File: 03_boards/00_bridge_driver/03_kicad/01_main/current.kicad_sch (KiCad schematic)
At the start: 20 parts, among them U12 AMC1311, U13 AMC1311

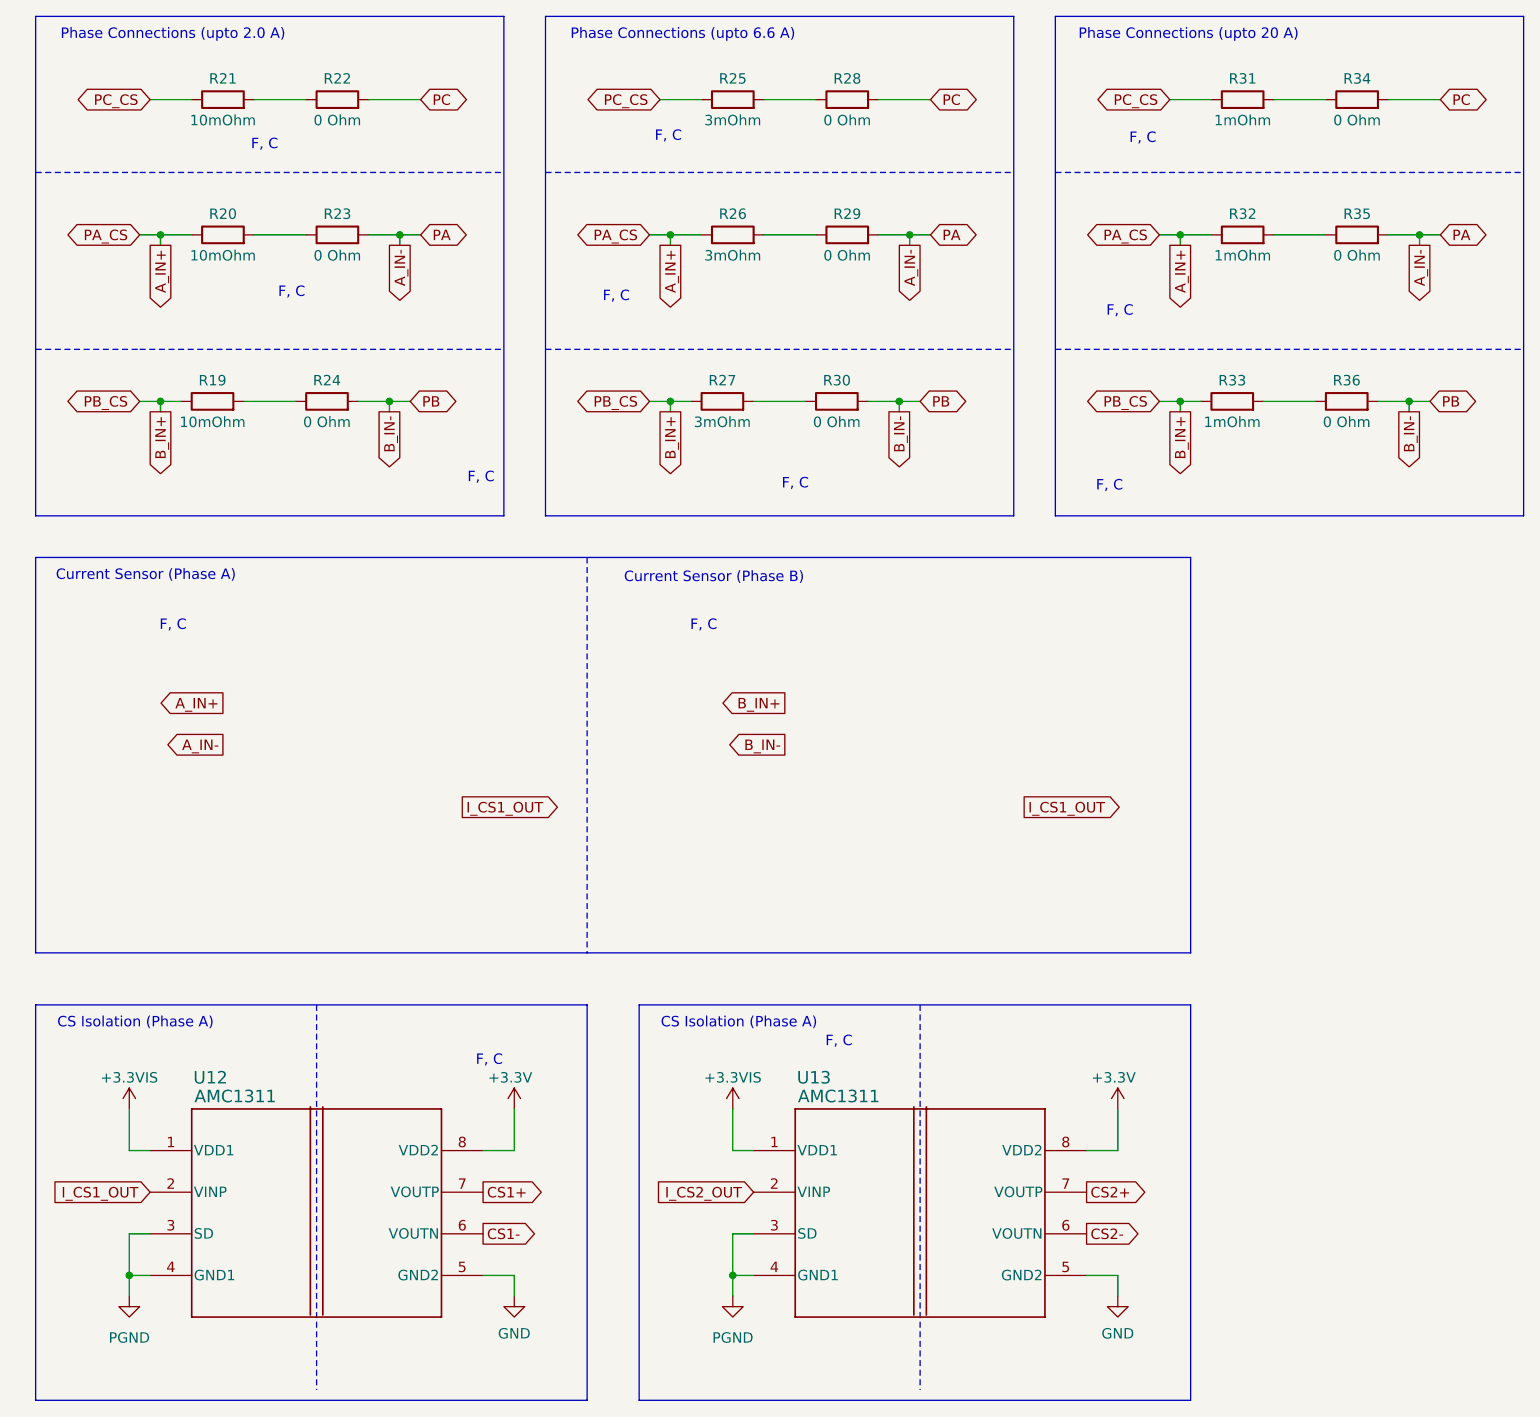
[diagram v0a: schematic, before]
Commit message: Nearly finished the schematic for driver board
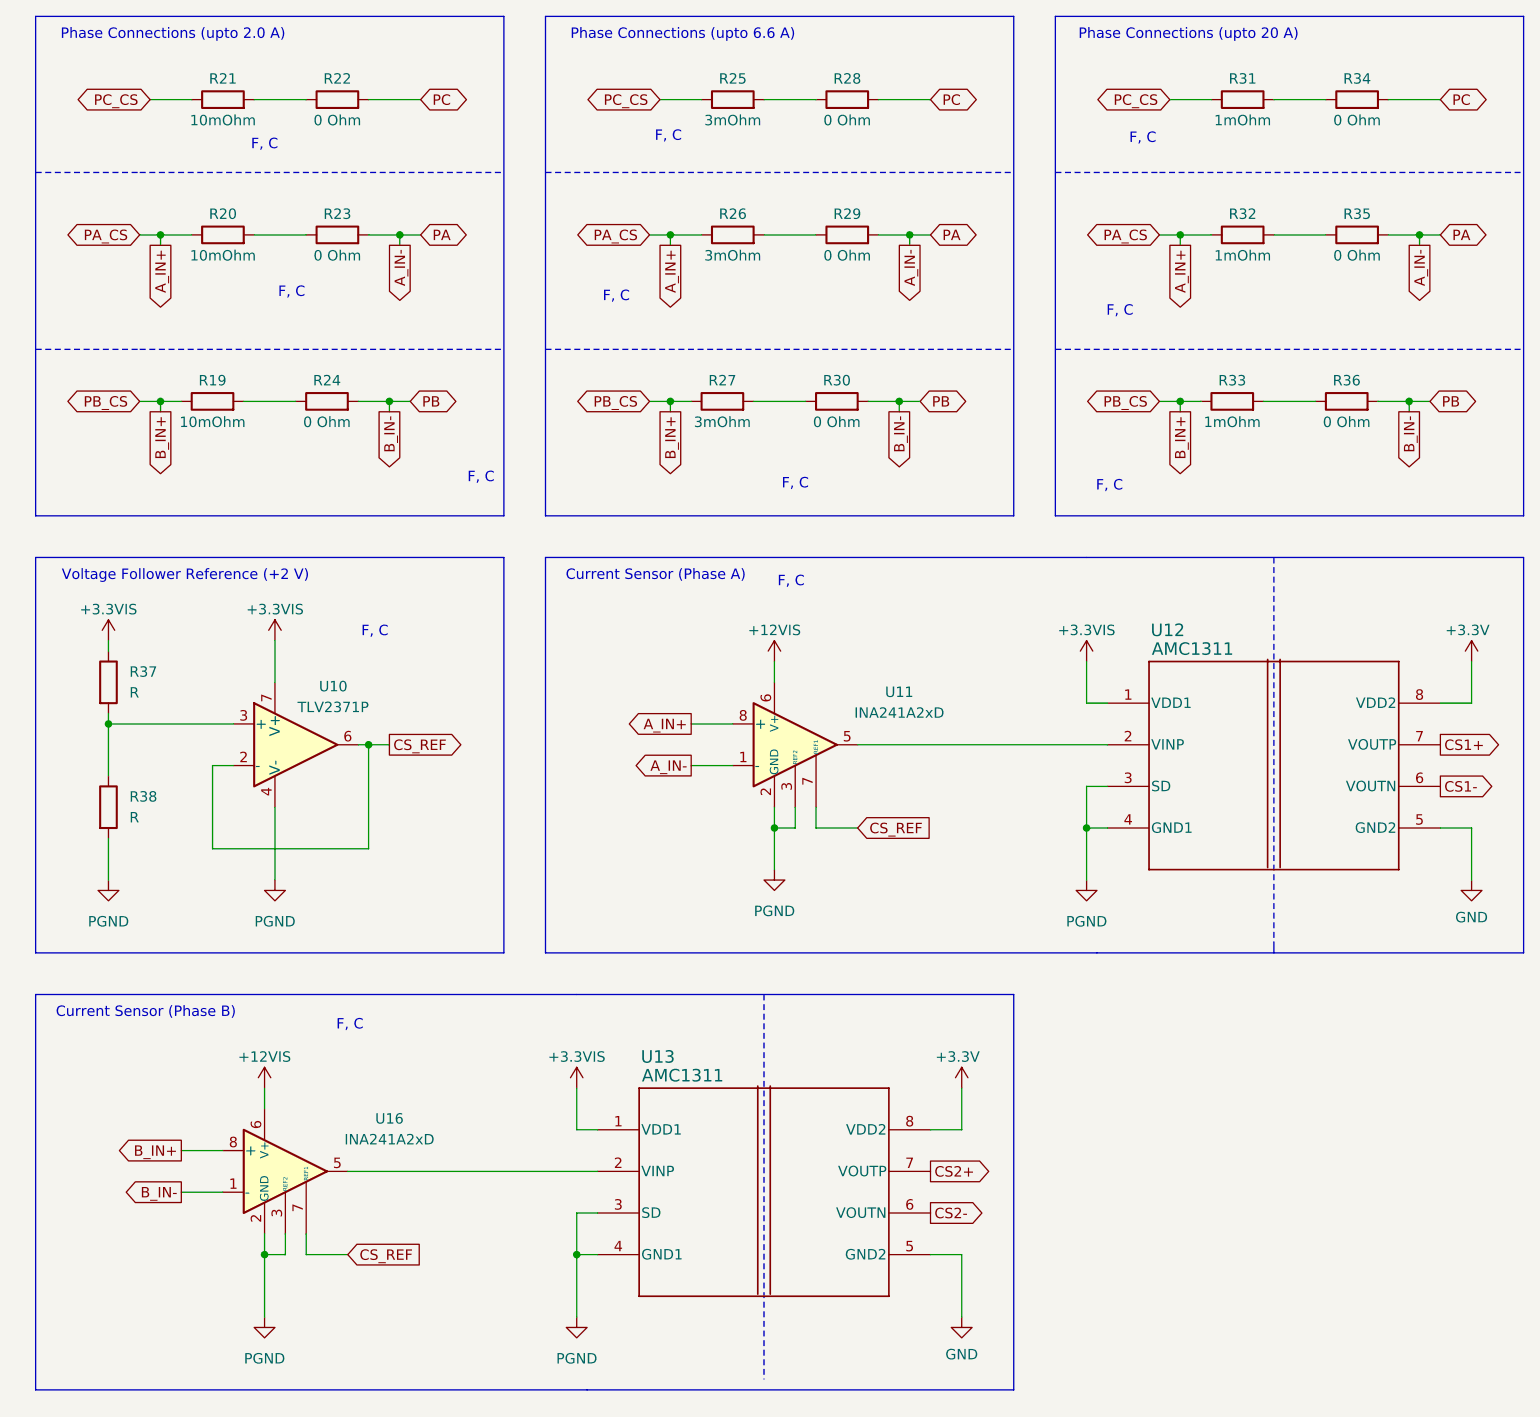
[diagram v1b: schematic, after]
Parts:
- added R37, R38: R, symbol Device:R
- added U10: TLV2371P, Package_DIP:DIP-8_W7.62mm, symbol Amplifier_Operational:TLV2371P
- added U11, U16: INA241A2xD, Package_SO:SOIC-8_3.9x4.9mm_P1.27mm, symbol Amplifier_Current:INA241A2xD
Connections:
- net +3.3VIS: now also R37.1, U10.7 (V+)
- net A_IN+: now also U11.8 (+)
- net A_IN-: now also U11.1 (-)
- net B_IN+: now also U16.8 (+)
- net B_IN-: now also U16.1 (-)
- net PGND: now also R38.2, U10.4 (V-), U11.2 (GND), U11.3 (REF2), U11.4 (GND), U16.2 (GND), U16.3 (REF2), U16.4 (GND)
- net I_CS1_OUT: no longer names the net of U12.2 (VINP)
- net I_CS1_OUT: now also U11.5
- net I_CS2_OUT: no longer names the net of U13.2 (VINP)
- net I_CS2_OUT: now also U16.5
- new net: R37.2, R38.1, U10.3 (+)
- new net +12VIS: U11.6 (V+), U16.6 (V+)
- new net CS_REF: U10.2 (-), U10.6, U11.7 (REF1), U16.7 (REF1)
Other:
- note added: "Voltage Follower Reference (+2 V)"
- note removed: "CS Isolation (Phase A)"
- moved on the sheet: U12, U13

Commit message: Finished Driver Board Schematic.
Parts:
- removed R37, R38: R, symbol Device:R
- removed U10: TLV2371P, Package_DIP:DIP-8_W7.62mm, symbol Amplifier_Operational:TLV2371P
- added C28: 10uF, symbol Device:C
- added U10: REF3020, Package_TO_SOT_SMD:SOT-23, symbol Reference_Voltage:REF3020
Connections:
- net +3.3VIS: now also C28.1, U10.1 (IN)
- net CS_REF: now also U10.2 (OUT)
- net PGND: now also C28.2, U10.3 (GND)

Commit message: More footprint selection. YAY
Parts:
- R19, R20, R21, R22, R23, R24, R25, R26, R27, R28, R29, R30, R31, R32, R33, R34, R35, R36: footprint (none) -> Resistor_SMD:R_2512_6332Metric
- U12, U13: footprint DWV0008A -> AMC1311DWVR:DWV0008A
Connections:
- net A_IN-: now also R20.2, R23.1, R26.2, R29.1, R32.2, R35.1; no longer R23.2, R29.2, R35.2
- net B_IN-: now also R19.2, R24.1, R27.2, R30.1, R33.2, R36.1; no longer R24.2, R30.2, R36.2
- new net PA: R23.2, R29.2, R35.2
- new net PB: R24.2, R30.2, R36.2
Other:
- note removed: "F, C"
- moved on the sheet: R22, R23, R24, R28, R29, R30, R34, R35, R36

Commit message: Footprints finished and hence initial BOM based on footprints is also
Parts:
- C28: footprint (none) -> Capacitor_SMD:C_1206_3216Metric
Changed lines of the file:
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@@
 			)
 		)
-		(property "Footprint" ""
+		(property "Footprint" "Capacitor_SMD:C_1206_3216Metric"
 			(at 25.0952 113.03 0)
 			(hide yes)

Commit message: Made it clear the values and updated the schematics.
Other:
- note added: "Phase Connections (upto 16.6 A (PEAK))"
- note added: "Phase Connections (upto 30 A (PEAK))"
- note added: "Phase Connections (upto 5.0 A (PEAK))"
- note removed: "Phase Connections (upto 2.0 A)"
- note removed: "Phase Connections (upto 20 A)"
- note removed: "Phase Connections (upto 6.6 A)"
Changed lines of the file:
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@@
 		(rev "0")
 	)
-	(text "Phase Connections (upto 20 A)\n"
+	(text "Phase Connections (upto 30 A (PEAK))\n"
 		(exclude_from_sim no)
-		(at 157.226 18.796 0)
+		(at 161.036 18.796 0)
 		(effects
 			(font
@@
 		)
 	)
-	(text "Phase Connections (upto 2.0 A)\n"
+	(text "Phase Connections (upto 5.0 A (PEAK))\n"
 		(exclude_from_sim no)
-		(at 33.274 18.796 0)
+		(at 36.83 18.796 0)
 		(effects
 			(font
@@
 		)
 	)
-	(text "Phase Connections (upto 6.6 A)\n"
+	(text "Phase Connections (upto 16.6 A (PEAK))\n"
 		(exclude_from_sim no)
-		(at 95.504 18.796 0)
+		(at 99.822 18.796 0)
 		(effects
 			(font

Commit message: Initial PCB modelling work
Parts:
- removed R22, R23, R24, R28, R29, R30, R34, R35, R36: 0 Ohm, Resistor_SMD:R_2512_6332Metric, symbol Device:R
- removed R25, R26, R27: 3mOhm, Resistor_SMD:R_2512_6332Metric, symbol Device:R
- removed R31, R32, R33: 1mOhm, Resistor_SMD:R_2512_6332Metric, symbol Device:R
- R19, R20, R21: value 10mOhm -> 5mOhm
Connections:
- net PC_CS is gone; now on net C_IN+: R21.1
- net PB: now also R19.2
- net C_IN-: now reaches R21.2
- net C_IN-: now also U16.1 (-)
- net B_IN+ renamed C_IN+
- net C_IN+: no longer R19.1
- removed net B_IN-: R19.2, U16.1 (-)
- new net PB_CS: R19.1
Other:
- note added: "Current Sensor (Phase C)"
- note added: "Phase Connections (upto 10 A (PEAK))"
- note added: "Voltage Reference (+2 V)"
- note removed: "Current Sensor (Phase B)"
- note removed: "Phase Connections (upto 16.6 A (PEAK))"
- note removed: "Phase Connections (upto 30 A (PEAK))"
- note removed: "Phase Connections (upto 5.0 A (PEAK))"
- note removed: "Voltage Follower Reference (+2 V)"
- moved on the sheet: C28, R19, R20, R21, U10, U11, U12, U13, U16
